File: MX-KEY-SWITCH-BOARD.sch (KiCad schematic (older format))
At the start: 0 parts

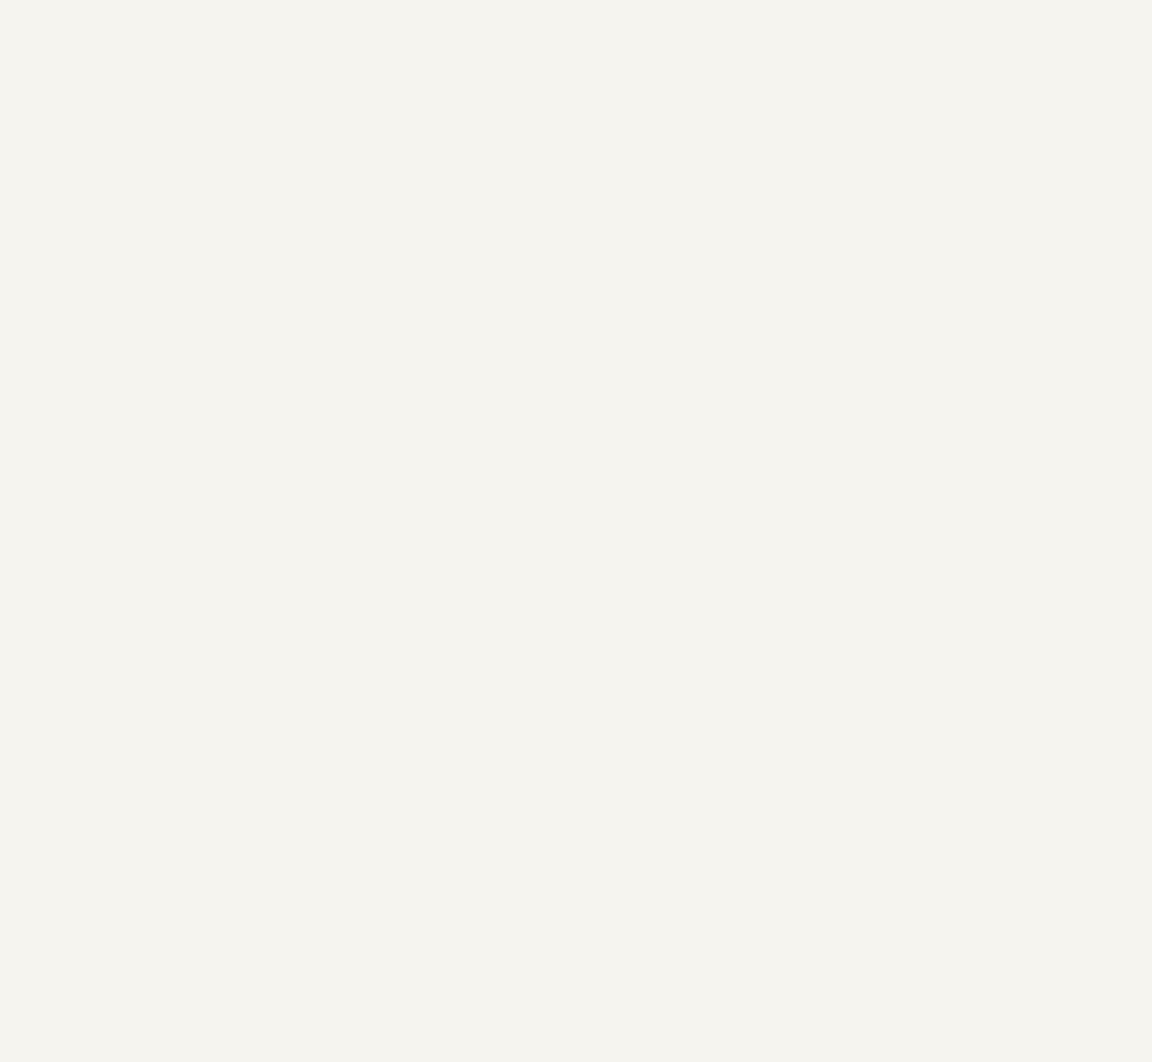
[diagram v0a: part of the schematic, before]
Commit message: Switching design to add headers to all four sides.
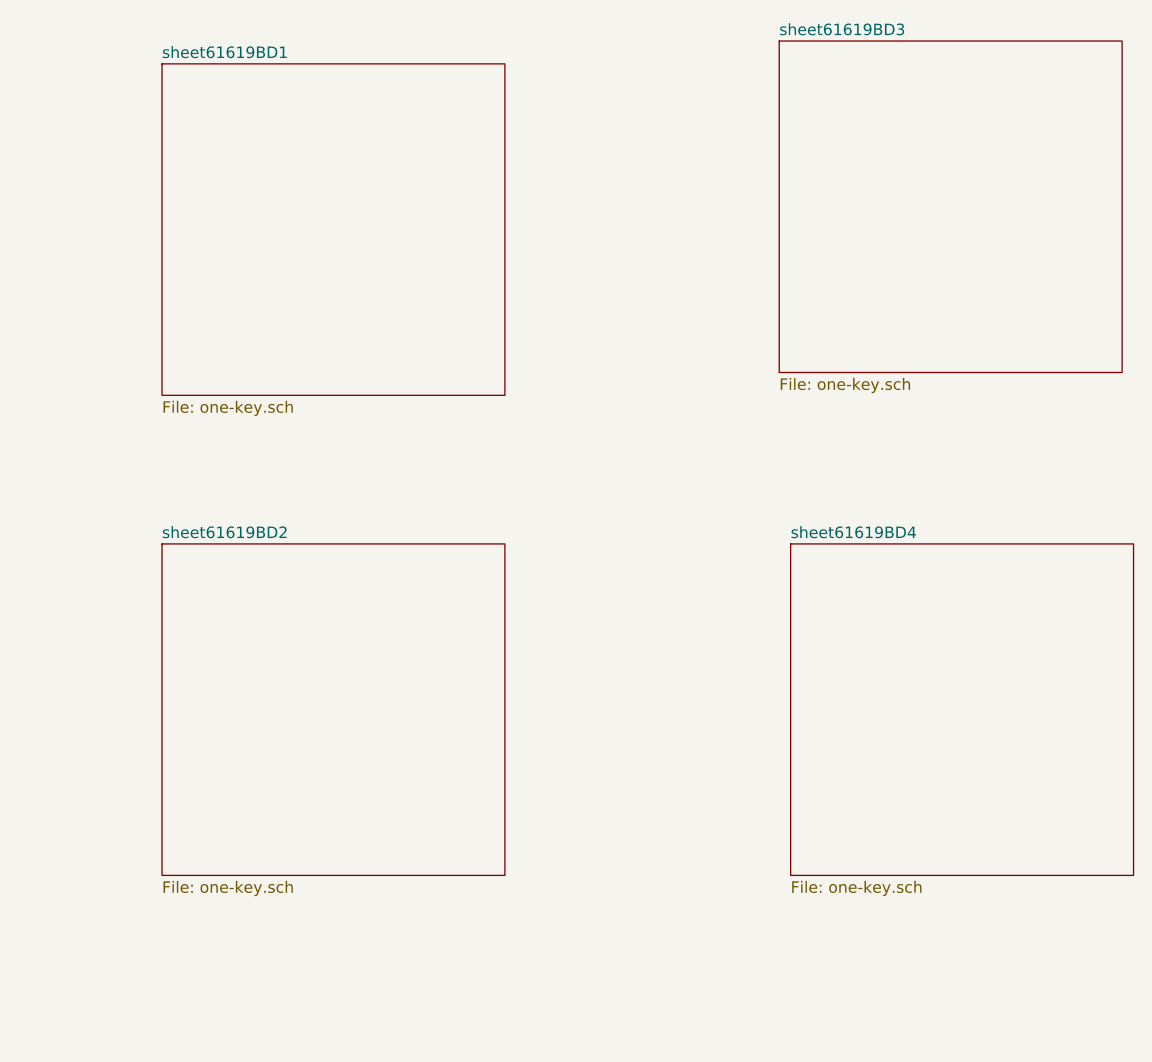
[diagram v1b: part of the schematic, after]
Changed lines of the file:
@@
 $Descr A4 11693 8268
 encoding utf-8
-Sheet 1 13
+Sheet 1 17
 Title ""
 Date ""
@@
 F1 "one-key.sch" 50
 $EndSheet
+$Sheet
+S 12150 1250 1500 1450
+U 61619BD6
+F0 "sheet61619BD1" 50
+F1 "one-key.sch" 50
+$EndSheet
+$Sheet
+S 12150 3350 1500 1450
+U 61619BD8
+F0 "sheet61619BD2" 50
+F1 "one-key.sch" 50
+$EndSheet
+$Sheet
+S 14850 1150 1500 1450
+U 61619BDA
+F0 "sheet61619BD3" 50
+F1 "one-key.sch" 50
+$EndSheet
+$Sheet
+S 14900 3350 1500 1450
+U 61619BDC
+F0 "sheet61619BD4" 50
+F1 "one-key.sch" 50
+$EndSheet
